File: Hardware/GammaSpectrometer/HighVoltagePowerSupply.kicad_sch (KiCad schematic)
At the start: 59 parts, among them J1 power supply, J2 Conn_01x07_Female, Q1 AOD2810, U1 MCP1416

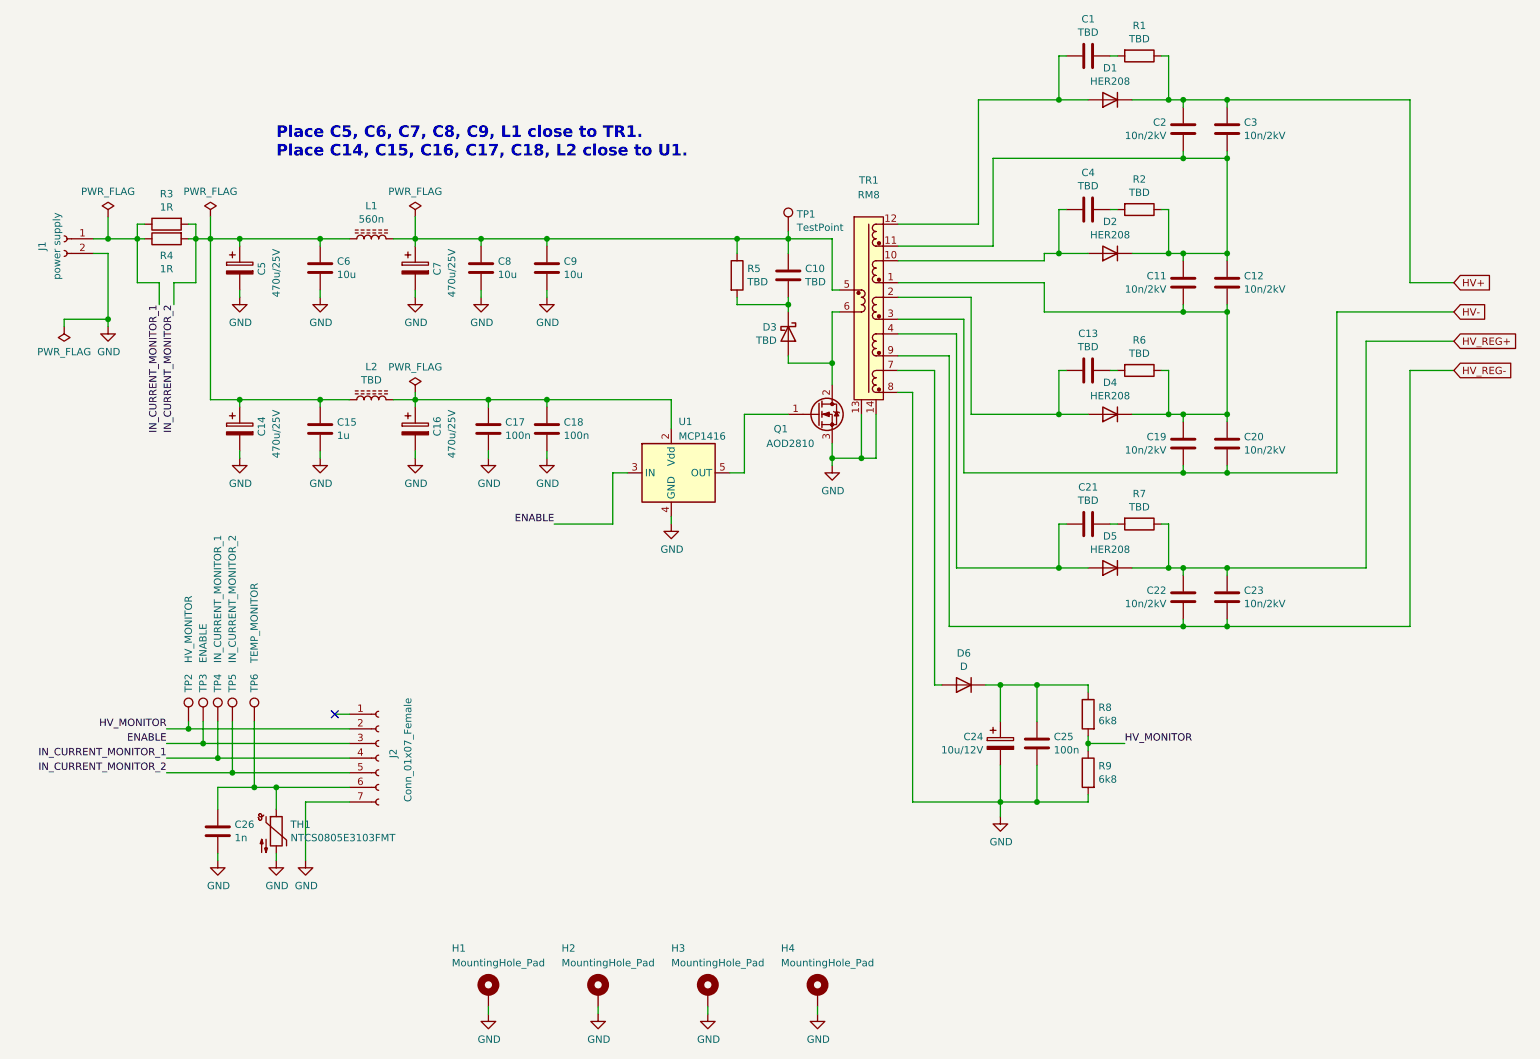
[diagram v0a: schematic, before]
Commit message: fixed footprints
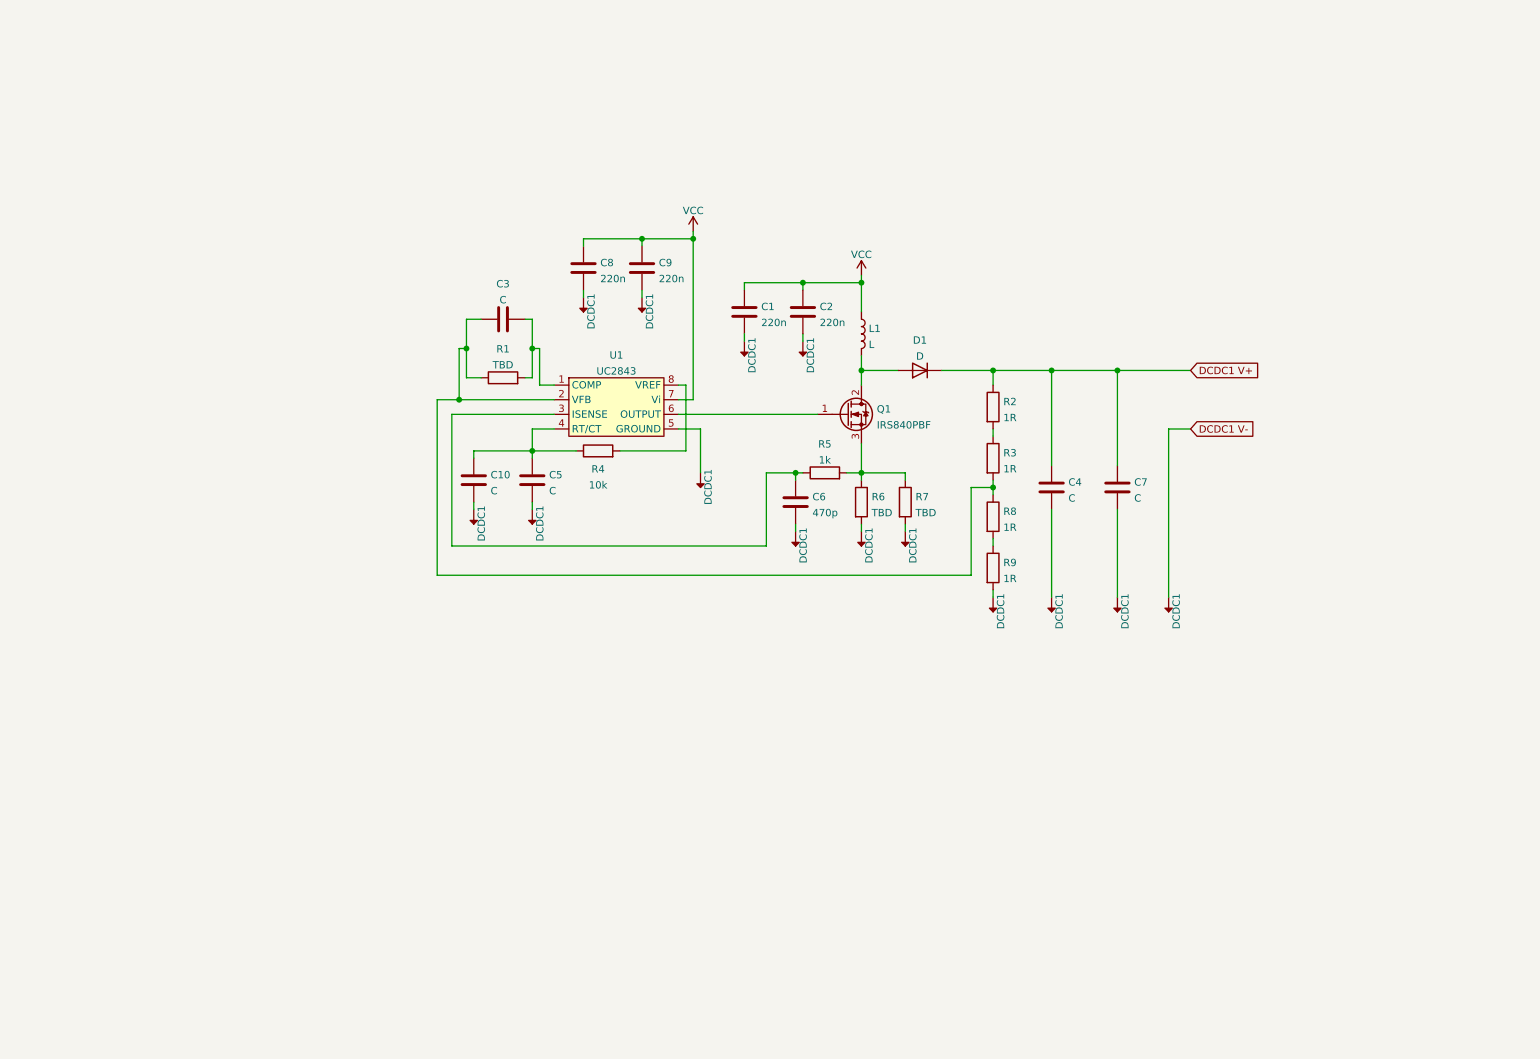
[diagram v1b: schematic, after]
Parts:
- removed C11, C12, C19, C20, C22, C23: 10n/2kV, Capacitor_THT:C_Disc_D7.5mm_W5.0mm_P7.50mm, symbol Device:C
- removed C13, C21: TBD, Capacitor_SMD:C_1206_3216Metric, symbol Device:C
- removed C14, C16, C5, C7: 470u/25V, Capacitor_SMD:CP_Elec_10x10, symbol Device:CP
- removed C15: 1u, Capacitor_SMD:C_1206_3216Metric, symbol Device:C
- removed C17, C18, C25: 100n, Capacitor_SMD:C_1206_3216Metric, symbol Device:C
- removed C24: 10u/12V, Capacitor_SMD:CP_Elec_10x10, symbol Device:CP
- removed C26: 1n, Capacitor_SMD:C_1206_3216Metric, symbol Device:C
- removed D2, D4, D5: HER208, Diode_SMD:D_MiniMELF, symbol Device:D
- removed D3: TBD, Diode_SMD:D_MiniMELF, symbol Device:D_Schottky
- removed D6: D, Diode_SMD:D_MiniMELF, symbol Device:D
- removed H1, H2, H3, H4: MountingHole_Pad, MountingHole:MountingHole_3.5mm_Pad, symbol Mechanical:MountingHole_Pad
- removed J1: power supply, Connector_PinSocket_2.54mm:PinSocket_1x02_P2.54mm_Vertical_SMD_Pin1Left, symbol Connector:Conn_01x02_Female
- removed J2: Conn_01x07_Female, Connector_PinSocket_2.54mm:PinSocket_1x07_P2.54mm_Vertical, symbol Connector:Conn_01x07_Female
- removed L1: 560n, Inductor_SMD:L_12x12mm_H6mm, symbol Device:L_Core_Ferrite
- removed L2: TBD, Inductor_SMD:L_12x12mm_H6mm, symbol Device:L_Core_Ferrite
- removed Q1: AOD2810, Package_TO_SOT_SMD:TO-252-2, symbol Transistor_FET:IRF740
- removed TH1: NTCS0805E3103FMT, Resistor_SMD:R_0805_2012Metric, symbol Device:Thermistor_NTC
- removed TP1: TestPoint, TestPoint:TestPoint_Pad_D1.5mm, symbol Connector:TestPoint
- removed TP2: HV_MONITOR, TestPoint:TestPoint_Pad_D1.5mm, symbol Connector:TestPoint
- removed TP3: ENABLE, TestPoint:TestPoint_Pad_D1.5mm, symbol Connector:TestPoint
- removed TP4: IN_CURRENT_MONITOR_1, TestPoint:TestPoint_Pad_D1.5mm, symbol Connector:TestPoint
- removed TP5: IN_CURRENT_MONITOR_2, TestPoint:TestPoint_Pad_D1.5mm, symbol Connector:TestPoint
- removed TP6: TEMP_MONITOR, TestPoint:TestPoint_Pad_D1.5mm, symbol Connector:TestPoint
- removed TR1: RM8, GammaSpectrometer:RM8, symbol GammaSpectrometer:RM8
- removed U1: MCP1416, Package_TO_SOT_SMD:SOT-23-5, symbol Driver_FET:MCP1416
- added C5: C, Capacitor_SMD:C_0805_2012Metric, symbol Device:C
- added C7: C, symbol Device:C
- added L1: L, symbol Device:L
- added Q1: IRS840PBF, Package_TO_SOT_THT:TO-220-3_Horizontal_TabUp, symbol Device:Q_NMOS_GDS
- added U1: UC2843, Package_SO:SO-8_3.9x4.9mm_P1.27mm, symbol GammaSpectrometer:UC2843
- C1: value TBD -> 220n; footprint Capacitor_SMD:C_1206_3216Metric -> Capacitor_SMD:C_0805_2012Metric
- C10: value TBD -> C; footprint Capacitor_SMD:C_1206_3216Metric -> Capacitor_SMD:C_0805_2012Metric
- C2: value 10n/2kV -> 220n; footprint Capacitor_THT:C_Disc_D7.5mm_W5.0mm_P7.50mm -> Capacitor_SMD:C_0805_2012Metric
- C3: value 10n/2kV -> C; footprint Capacitor_THT:C_Disc_D7.5mm_W5.0mm_P7.50mm -> Capacitor_SMD:C_0805_2012Metric
- C4: value TBD -> C; footprint Capacitor_SMD:C_1206_3216Metric -> (none)
- C6: value 10u -> 470p; footprint Capacitor_SMD:C_1206_3216Metric -> Capacitor_SMD:C_0805_2012Metric
- C8, C9: value 10u -> 220n; footprint Capacitor_SMD:C_1206_3216Metric -> Capacitor_SMD:C_0805_2012Metric
- D1: value HER208 -> D; footprint Diode_SMD:D_MiniMELF -> Diode_THT:D_DO-35_SOD27_P7.62mm_Horizontal
- R1: footprint Resistor_SMD:R_MELF_MMB-0207 -> Resistor_SMD:R_0805_2012Metric
- R2: value TBD -> 1R; footprint Resistor_SMD:R_MELF_MMB-0207 -> Resistor_THT:R_Axial_DIN0204_L3.6mm_D1.6mm_P7.62mm_Horizontal
- R3: footprint Resistor_SMD:R_1206_3216Metric -> Resistor_THT:R_Axial_DIN0204_L3.6mm_D1.6mm_P7.62mm_Horizontal
- R4: value 1R -> 10k; footprint Resistor_SMD:R_1206_3216Metric -> Resistor_SMD:R_0805_2012Metric
- R5: value TBD -> 1k; footprint Resistor_SMD:R_MELF_MMB-0207 -> Resistor_SMD:R_0805_2012Metric
- R6, R7: footprint Resistor_SMD:R_MELF_MMB-0207 -> Resistor_SMD:R_1206_3216Metric
- R8, R9: value 6k8 -> 1R; footprint Resistor_SMD:R_1206_3216Metric -> Resistor_SMD:R_0805_2012Metric
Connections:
- net HV_REG+ is gone; now on an unnamed net: R7.1
- net at C10.1: now also R4.1, C5.1, U1.4 (RT/CT); no longer R5.2
- net VCC: now reaches C8.2, C9.2
- net VCC: now also C1.2, C2.2, L1.1, U1.7 (Vi); no longer C10.2, R5.1
- net at R6.1: now also R5.2, Q1.3 (S)
- net DCDC1: now reaches R6.2
- net DCDC1: now also C1.1, C10.2, C2.1, C4.2, C6.2, C8.1, C9.1, R7.2, R9.2, C5.2, C7.2, U1.5 (GROUND)
- net DCDC1 V+: now reaches C4.1
- net DCDC1 V+: now also D1.1 (K), R2.1, C7.1
- net at D1.2 (A): now also L1.2, Q1.2 (D); no longer C1.1
- net at R8.1: now also C3.1, R1.1, R3.2, U1.2 (VFB)
- net at R1.2: now also C3.2, U1.1 (COMP); no longer C1.2
- net at R2.2: now also R3.1; no longer C4.2
- removed net GND: C6.1, C8.1, C9.1, R9.2
- removed net HV+: C2.2, C3.2, D1.1 (K), R1.1
- net HV_MONITOR: no longer names the net of R8.2, R9.1
- removed net IN_CURRENT_MONITOR_1: R3.1, R4.1
- removed net IN_CURRENT_MONITOR_2: C6.2, R3.2, R4.2
- new net: C6.1, R5.1, U1.3 (ISENSE)
- new net: Q1.1 (G), U1.6 (OUTPUT)
- new net: R4.2, U1.8 (VREF)
- no-connect marks 1 -> 0
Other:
- note removed: "Place C5, C6, C7, C8, C9, L1 close to TR1. Place C14, C15, C16, C17, C18, L2 close to U1."

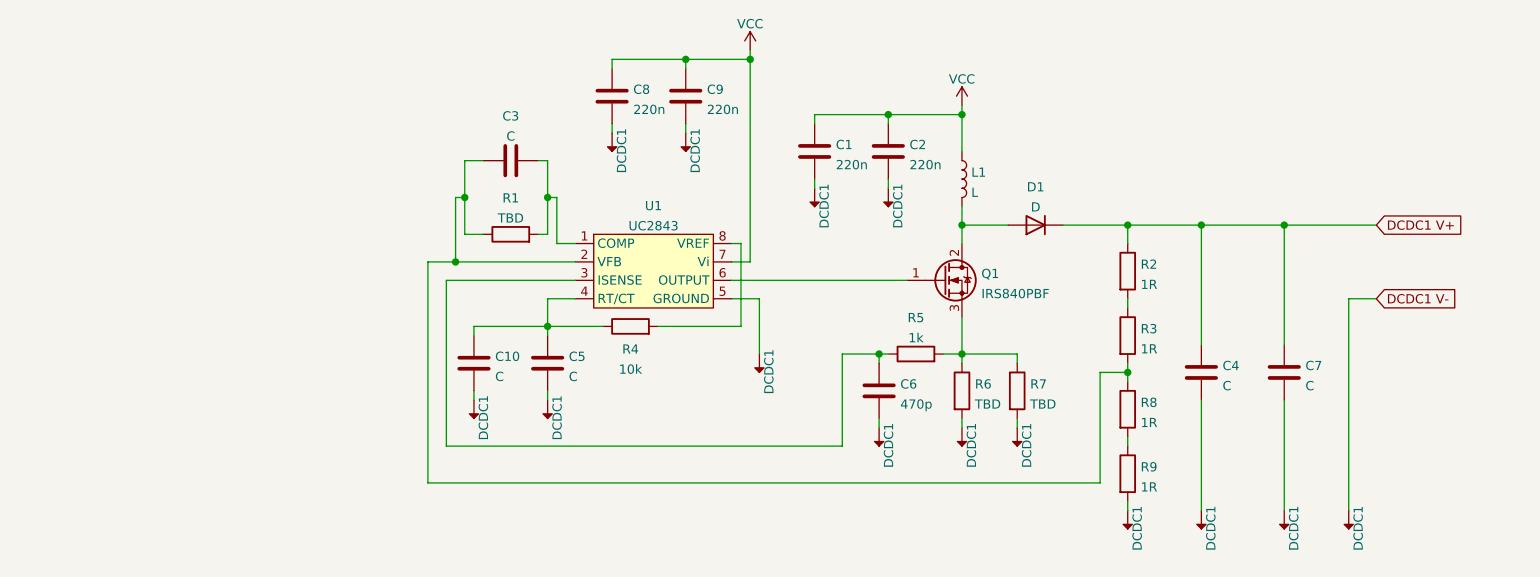
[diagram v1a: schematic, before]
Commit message: beggining draft of in-series hv power supply
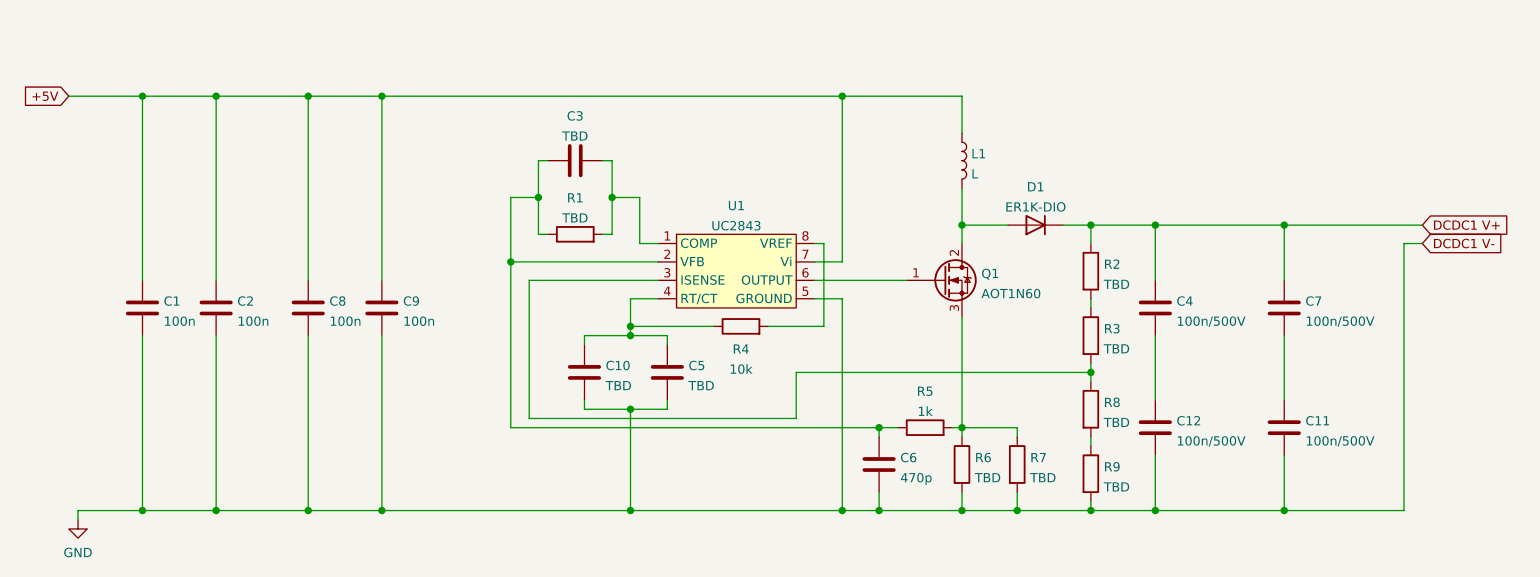
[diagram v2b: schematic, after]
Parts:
- added C11, C12: 100n/500V, Capacitor_THT:C_Disc_D5.0mm_W2.5mm_P5.00mm, symbol Device:C
- C1, C2, C8, C9: value 220n -> 100n
- C10, C3, C5: value C -> TBD
- C4, C7: value C -> 100n/500V; footprint (none) -> Capacitor_THT:C_Disc_D5.0mm_W2.5mm_P5.00mm; Store (none) -> https://www.tme.eu/pl/details/cc-104_500/kondensatory-ceram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
- D1: value D -> ER1K-DIO
- Q1: value IRS840PBF -> AOT1N60
- R2, R3: value 1R -> TBD; footprint Resistor_THT:R_Axial_DIN0204_L3.6mm_D1.6mm_P7.62mm_Horizontal -> Resistor_THT:R_Axial_DIN0204_L3.6mm_D1.6mm_P2.54mm_Vertical
- R6, R7: footprint Resistor_SMD:R_1206_3216Metric -> Resistor_THT:R_Axial_DIN0204_L3.6mm_D1.6mm_P1.90mm_Vertical
- R8, R9: value 1R -> TBD
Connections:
- net at C3.1, R1.1, U1.2 (VFB): now also C6.1, R5.1; no longer R3.2, R8.1
- net DCDC1 renamed GND
- net GND: now also C11.2, C12.2; no longer C4.2, C7.2
- net VCC renamed +5V
- new net: C11.1, C7.2
- new net: R3.2, R8.1, U1.3 (ISENSE)
- new net: C12.1, C4.2
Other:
- moved on the sheet: C1, C10, C2, C3, C5, C6, C8, C9, L1, R1, R2, R3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
